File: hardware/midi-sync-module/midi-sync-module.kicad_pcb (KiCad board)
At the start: 2 copper layers, 20 x 108 mm, 41 parts, among them J1 AudioJack2_SwitchT, J2 Conn_01x10_Male, J3 DIN-5_180degree, J4 Conn_02x05_Odd_Even, J5 Conn_02x05_Odd_Even, Q1 MMBT3904, U1 ISU0205S05, U2 6N137, U3 ADP7142AUJZ-3.3

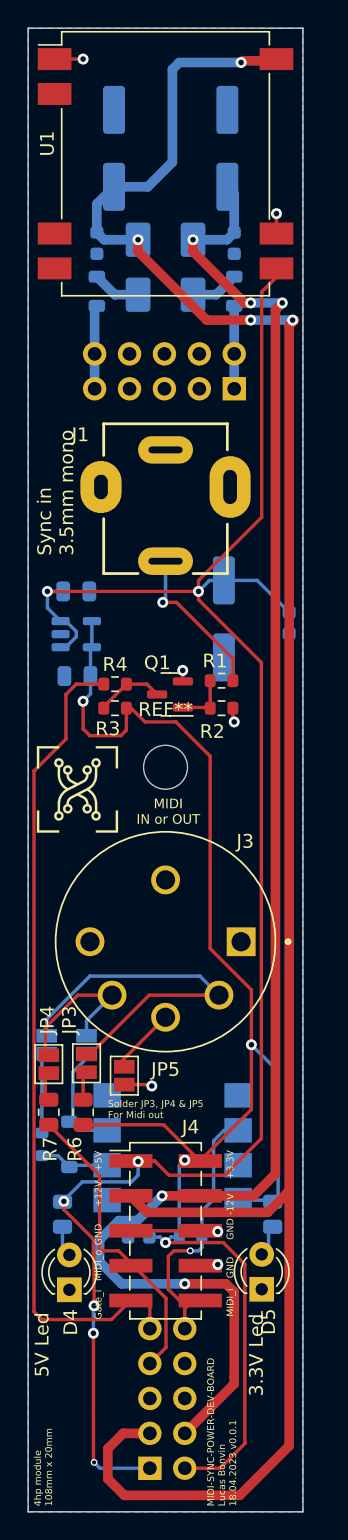
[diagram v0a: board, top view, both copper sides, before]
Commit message: update pbc to v0.0.2 (fix polarized cap C3 and some texts) and panel c
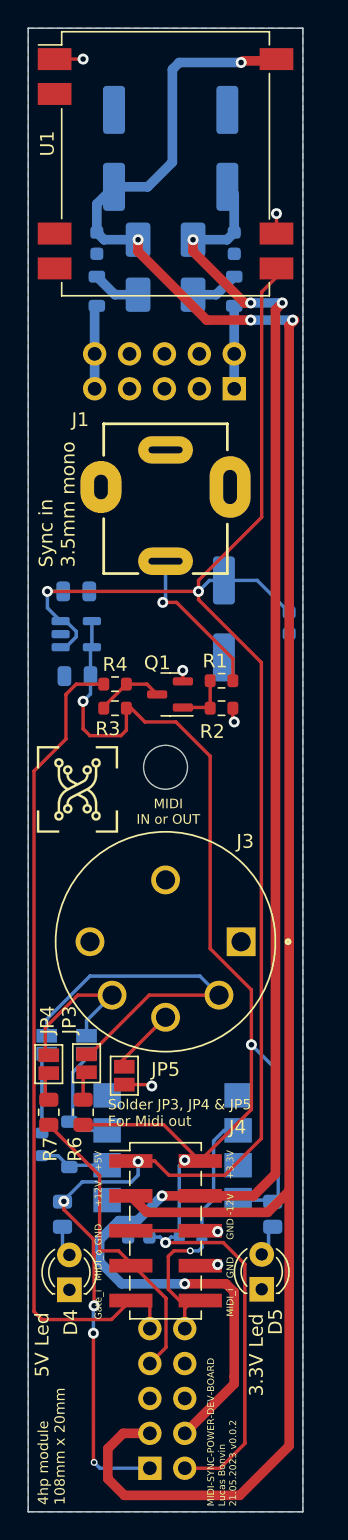
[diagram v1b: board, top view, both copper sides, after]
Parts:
- R10, R9: value R -> 330
- R6: value R -> 30
- R7: value R -> 10
- turned C4 to -90 degrees
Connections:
- C4 pad 1: -12V -> GND
- C4 pad 2: GND -> -12V
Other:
- board text added: "MIDI-SYNC-POWER-DEV-BOARD Lucas Bonvin 21.05.2023 v0.0.2"
- board text removed: "MIDI-SYNC-POWER-DEV-BOARD Lucas Bonvin 18.04.2023 v0.0.1"
